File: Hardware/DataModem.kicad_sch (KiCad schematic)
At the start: 33 parts, among them J1 5V, J2 SERIAL, J3 DB9 FEMALE (DCE), J4 OUT, J5 IN, Q1 2N3904, U1 MAX232, U2 LM555, U3 LM555, U4 LM358

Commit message: Add PCB
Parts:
- C1, C10, C11, C2, C3, C4, C5, C6, C7, C8, C9: footprint (none) -> Capacitor_THT:C_Disc_D5.0mm_W2.5mm_P2.50mm
- J1: footprint (none) -> Connector_BarrelJack:BarrelJack_CUI_PJ-063AH_Horizontal
- J2: footprint (none) -> Connector_PinHeader_2.54mm:PinHeader_1x04_P2.54mm_Horizontal
- J4, J5: footprint (none) -> DataModem Parts:SWITCHCRAFT_PJRAN1X1U02X
- R1, R2, R3, R4, R5, R6, R7, R8, R9: footprint (none) -> Resistor_THT:R_Axial_DIN0204_L3.6mm_D1.6mm_P5.08mm_Horizontal
- RV1, RV2: footprint (none) -> DataModem Parts:3386F-1-103LF
- U1: footprint (none) -> Package_DIP:DIP-16_W7.62mm_Socket_LongPads
- U4: footprint (none) -> Package_DIP:DIP-8_W7.62mm
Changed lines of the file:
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@@
 			)
 		)
-		(property "Footprint" ""
+		(property "Footprint" "DataModem Parts:SWITCHCRAFT_PJRAN1X1U02X"
 			(at 257.81 130.81 0)
 			(effects
@@
 			)
 		)
-		(property "Footprint" ""
+		(property "Footprint" "Resistor_THT:R_Axial_DIN0204_L3.6mm_D1.6mm_P5.08mm_Horizontal"
 			(at 189.23 138.938 90)
 			(effects
@@
 			)
 		)
-		(property "Footprint" ""
+		(property "Footprint" "Capacitor_THT:C_Disc_D5.0mm_W2.5mm_P2.50mm"
 			(at 145.7452 129.54 0)
 			(effects
@@
 			)
 		)
-		(property "Footprint" ""
+		(property "Footprint" "Capacitor_THT:C_Disc_D5.0mm_W2.5mm_P2.50mm"
 			(at 120.3452 140.97 0)
 			(effects
@@
 			)
 		)
-		(property "Footprint" ""
+		(property "Footprint" "Capacitor_THT:C_Disc_D5.0mm_W2.5mm_P2.50mm"
 			(at 123.19 145.0848 0)
 			(effects
@@
 			)
 		)
-		(property "Footprint" ""
+		(property "Footprint" "Package_DIP:DIP-8_W7.62mm"
 			(at 215.9 55.88 0)
 			(effects
@@
 			)
 		)
-		(property "Footprint" ""
+		(property "Footprint" "Resistor_THT:R_Axial_DIN0204_L3.6mm_D1.6mm_P5.08mm_Horizontal"
 			(at 224.282 101.6 90)
 			(effects
@@
 			)
 		)
-		(property "Footprint" ""
+		(property "Footprint" "Connector_BarrelJack:BarrelJack_CUI_PJ-063AH_Horizontal"
 			(at 45.72 48.006 0)
 			(effects
@@
 			)
 		)
-		(property "Footprint" ""
+		(property "Footprint" "Capacitor_THT:C_Disc_D5.0mm_W2.5mm_P2.50mm"
 			(at 123.19 152.7048 0)
 			(effects
@@
 			)
 		)
-		(property "Footprint" ""
+		(property "Footprint" "Resistor_THT:R_Axial_DIN0204_L3.6mm_D1.6mm_P5.08mm_Horizontal"
 			(at 234.442 101.6 90)
 			(effects
@@
 			)
 		)
-		(property "Footprint" ""
+		(property "Footprint" "Resistor_THT:R_Axial_DIN0204_L3.6mm_D1.6mm_P5.08mm_Horizontal"
 			(at 121.412 49.53 90)
 			(effects
@@
 			)
 		)
-		(property "Footprint" ""
+		(property "Footprint" "Capacitor_THT:C_Disc_D5.0mm_W2.5mm_P2.50mm"
 			(at 68.2752 53.34 0)
 			(effects
@@
 			)
 		)
-		(property "Footprint" ""
+		(property "Footprint" "Package_DIP:DIP-8_W7.62mm"
 			(at 46.99 168.91 0)
 			(effects
@@
 			)
 		)
-		(property "Footprint" ""
+		(property "Footprint" "Package_DIP:DIP-8_W7.62mm"
 			(at 214.63 128.27 0)
 			(effects
@@
 			)
 		)
-		(property "Footprint" ""
+		(property "Footprint" "DataModem Parts:SWITCHCRAFT_PJRAN1X1U02X"
 			(at 257.81 55.88 0)
 			(effects
@@
 			)
 		)
-		(property "Footprint" ""
+		(property "Footprint" "Resistor_THT:R_Axial_DIN0204_L3.6mm_D1.6mm_P5.08mm_Horizontal"
 			(at 224.282 143.51 90)
 			(effects
@@
 			)
 		)
-		(property "Footprint" ""
+		(property "Footprint" "Capacitor_THT:C_Disc_D5.0mm_W2.5mm_P2.50mm"
 			(at 241.3 131.7752 0)
 			(effects
@@
 			)
 		)
-		(property "Footprint" ""
+		(property "Footprint" "Capacitor_THT:C_Disc_D5.0mm_W2.5mm_P2.50mm"
 			(at 247.65 54.9148 0)
 			(effects
@@
 			)
 		)
-		(property "Footprint" ""
+		(property "Footprint" "Resistor_THT:R_Axial_DIN0204_L3.6mm_D1.6mm_P5.08mm_Horizontal"
 			(at 234.442 143.51 90)
 			(effects
@@
 					(size 1.27 1.27)
 				)
-				(hide yes)
 			)
 		)
@@
 			)
 		)
-		(property "Footprint" ""
+		(property "Footprint" "Capacitor_THT:C_Disc_D5.0mm_W2.5mm_P2.50mm"
 			(at 68.2752 140.97 0)
 			(effects
@@
 			)
 		)
-		(property "Footprint" ""
+		(property "Footprint" "DataModem Parts:3386F-1-103LF"
 			(at 201.93 137.16 0)
 			(effects
@@
 			)
 		)
-		(property "Footprint" ""
+		(property "Footprint" "Package_DIP:DIP-16_W7.62mm_Socket_LongPads"
 			(at 93.98 182.88 0)
 			(effects
@@
 			)
 		)
-		(property "Footprint" ""
+		(property "Footprint" "Resistor_THT:R_Axial_DIN0204_L3.6mm_D1.6mm_P5.08mm_Horizontal"
 			(at 121.412 29.21 90)
 			(effects
@@
 			)
 		)
-		(property "Footprint" ""
+		(property "Footprint" "Connector_PinHeader_2.54mm:PinHeader_1x04_P2.54mm_Horizontal"
 			(at 44.45 73.66 0)
 			(effects
@@
 			)
 		)
-		(property "Footprint" ""
+		(property "Footprint" "Resistor_THT:R_Axial_DIN0204_L3.6mm_D1.6mm_P5.08mm_Horizontal"
 			(at 160.782 101.6 90)
 			(effects
@@
 			)
 		)
-		(property "Footprint" ""
+		(property "Footprint" "DataModem Parts:3386F-1-103LF"
 			(at 162.56 53.34 0)
 			(effects
@@
 			)
 		)
-		(property "Footprint" ""
+		(property "Footprint" "Capacitor_THT:C_Disc_D5.0mm_W2.5mm_P2.50mm"
 			(at 161.5948 128.27 0)
 			(effects
@@
 			)
 		)
-		(property "Footprint" ""
+		(property "Footprint" "Capacitor_THT:C_Disc_D5.0mm_W2.5mm_P2.50mm"
 			(at 124.1552 68.58 0)
 			(effects
@@
 			)
 		)
-		(property "Footprint" ""
+		(property "Footprint" "Resistor_THT:R_Axial_DIN0204_L3.6mm_D1.6mm_P5.08mm_Horizontal"
 			(at 174.752 101.6 90)
 			(effects
@@
 			)
 		)
-		(property "Footprint" ""
+		(property "Footprint" "Capacitor_THT:C_Disc_D5.0mm_W2.5mm_P2.50mm"
 			(at 145.7452 66.04 0)
 			(effects

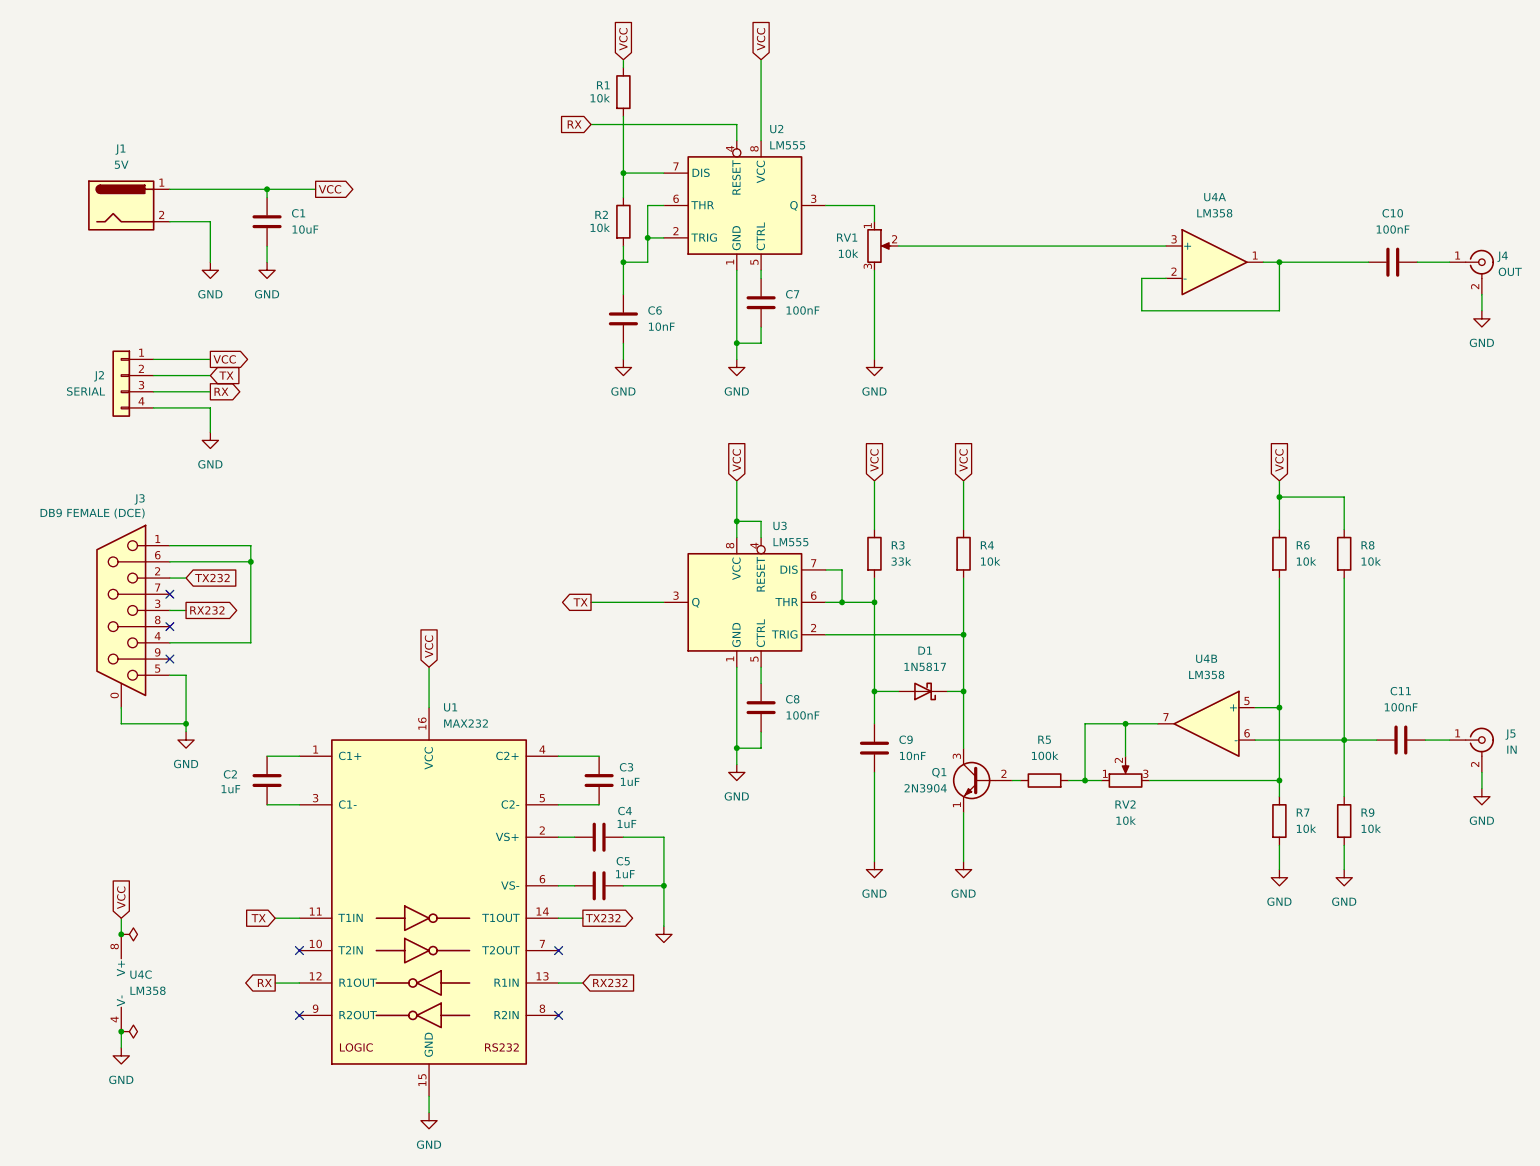
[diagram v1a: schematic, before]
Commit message: Add screw terminal for power input
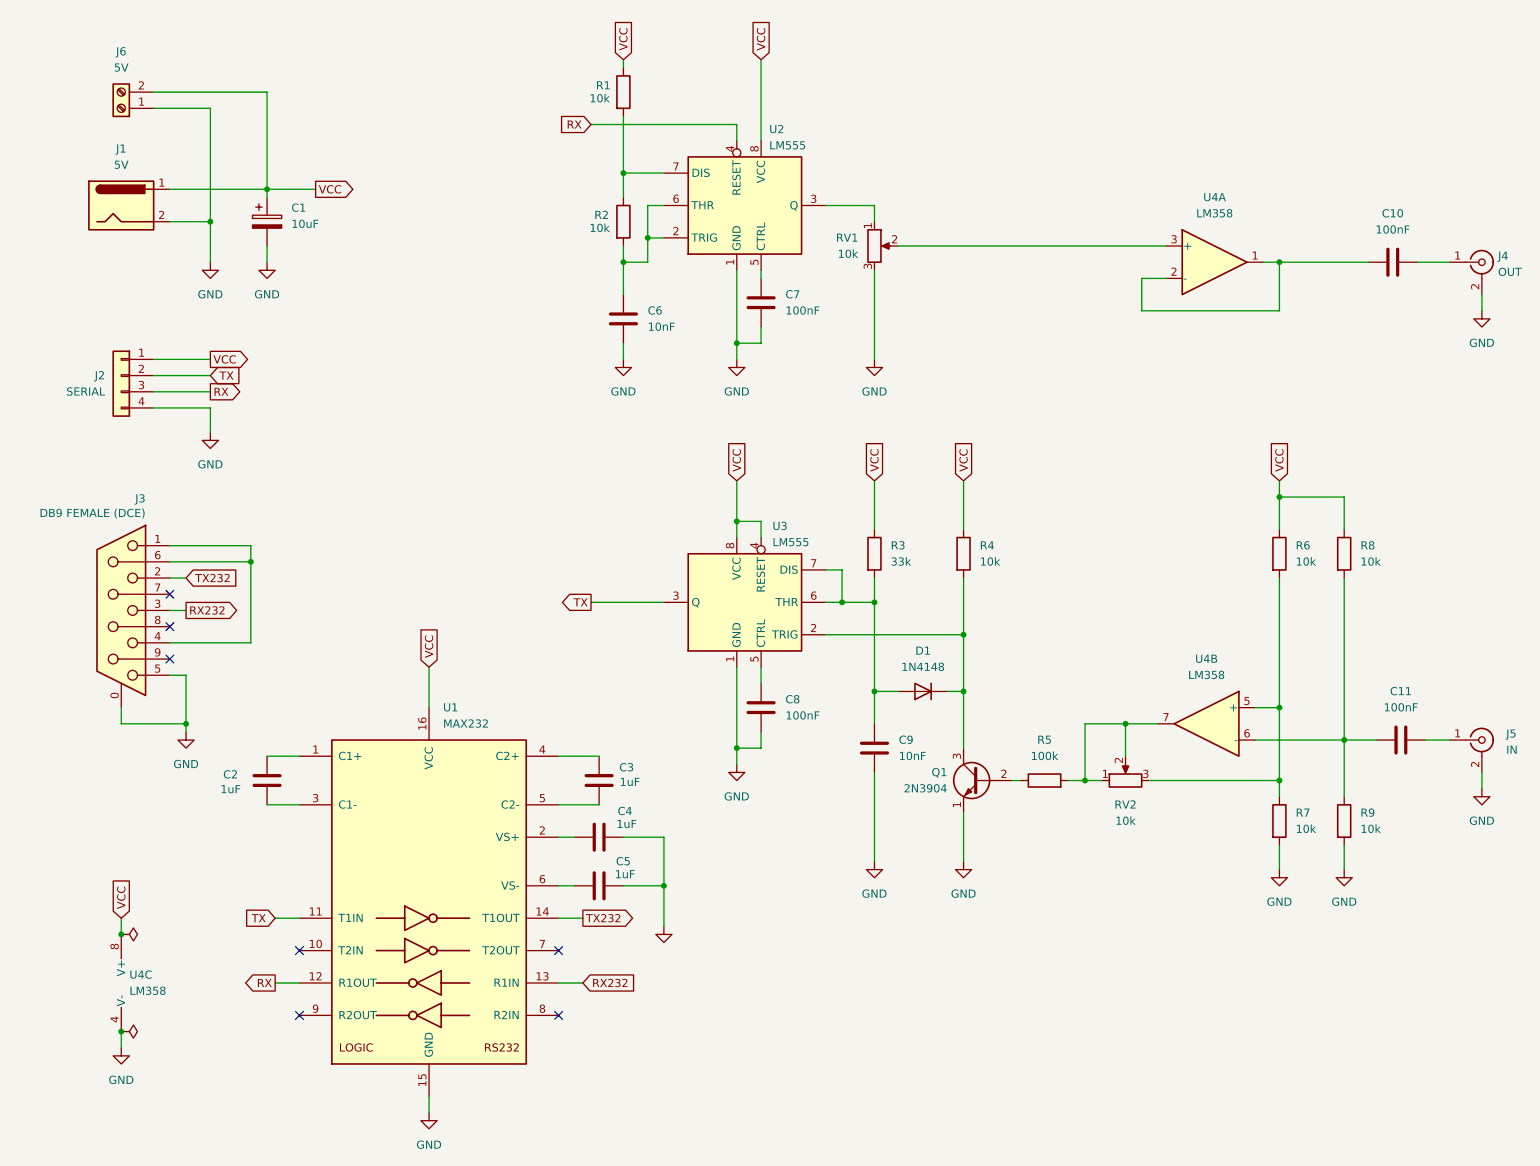
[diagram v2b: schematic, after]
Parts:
- added J6: 5V, TerminalBlock_Phoenix:TerminalBlock_Phoenix_MKDS-1,5-2-5.08_1x02_P5.08mm_Horizontal, symbol Connector:Screw_Terminal_01x02
- C1: footprint Capacitor_THT:C_Disc_D5.0mm_W2.5mm_P2.50mm -> Capacitor_THT:CP_Radial_D5.0mm_P2.50mm; symbol Device:C -> Device:C_Polarized
- D1: value 1N5817 -> 1N4148; footprint Diode_THT:D_DO-41_SOD81_P10.16mm_Horizontal -> Diode_THT:D_DO-35_SOD27_P7.62mm_Horizontal; symbol Diode:1N5817 -> Diode:1N4148
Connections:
- net GND: now also J6.1 (Pin_1)
- net VCC: now also J6.2 (Pin_2)
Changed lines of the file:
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@@
 	)
 	(junction
+		(at 58.42 49.53)
+		(diameter 0)
+		(color 0 0 0 0)
+	)
+	(junction
 		(at 195.58 137.16)
 		(diameter 0)
@@
 	(wire
 		(pts
+			(xy 58.42 31.75) (xy 58.42 49.53)
+		)
+		(stroke
+			(width 0)
+			(type default)
+		)
+	)
+	(wire
+		(pts
 			(xy 162.56 46.99) (xy 162.56 49.53)
 		)
@@
 	(wire
 		(pts
+			(xy 67.31 29.21) (xy 67.31 44.45)
+		)
+		(stroke
+			(width 0)
+			(type default)
+		)
+	)
+	(wire
+		(pts
 			(xy 157.48 109.22) (xy 154.94 109.22)
 		)
@@
 	(wire
 		(pts
+			(xy 49.53 31.75) (xy 58.42 31.75)
+		)
+		(stroke
+			(width 0)
+			(type default)
+		)
+	)
+	(wire
+		(pts
 			(xy 44.45 128.27) (xy 54.61 128.27)
 		)
@@
 	(wire
 		(pts
+			(xy 49.53 29.21) (xy 67.31 29.21)
+		)
+		(stroke
+			(width 0)
+			(type default)
+		)
+	)
+	(wire
+		(pts
 			(xy 226.06 92.71) (xy 226.06 97.79)
 		)
@@
 	)
 	(symbol
-		(lib_id "Diode:1N5817")
+		(lib_id "Diode:1N4148")
 		(at 170.18 123.19 180)
 		(unit 1)
@@
 		(fields_autoplaced yes)
 		(property "Reference" "D1"
-			(at 170.4975 116.84 0)
+			(at 170.18 116.84 0)
 			(effects
 				(font
@@
 			)
 		)
-		(property "Value" "1N5817"
-			(at 170.4975 119.38 0)
+		(property "Value" "1N4148"
+			(at 170.18 119.38 0)
 			(effects
 				(font
@@
 			)
 		)
-		(property "Footprint" "Diode_THT:D_DO-41_SOD81_P10.16mm_Horizontal"
-			(at 170.18 118.745 0)
+		(property "Footprint" "Diode_THT:D_DO-35_SOD27_P7.62mm_Horizontal"
+			(at 170.18 123.19 0)
 			(effects
 				(font
@@
 			)
 		)
-		(property "Datasheet" "http://www.vishay.com/docs/88525/1n5817.pdf"
+		(property "Datasheet" "https://assets.nexperia.com/documents/data-sheet/1N4148_1N4448.pdf"
 			(at 170.18 123.19 0)
 			(effects
@@
 			)
 		)
-		(property "Description" "20V 1A Schottky Barrier Rectifier Diode, DO-41"
+		(property "Description" "100V 0.15A standard switching diode, DO-35"
+			(at 170.18 123.19 0)
+			(effects
+				(font
+					(size 1.27 1.27)
+				)
+				(hide yes)
+			)
+		)
+		(property "Sim.Device" "D"
+			(at 170.18 123.19 0)
+			(effects
+				(font
+					(size 1.27 1.27)
+				)
+				(hide yes)
+			)
+		)
+		(property "Sim.Pins" "1=K 2=A"
 			(at 170.18 123.19 0)
 			(effects
@@
 	)
 	(symbol
-		(lib_id "Device:C")
+		(lib_id "Device:C_Polarized")
 		(at 67.31 49.53 0)
 		(unit 1)
@@
 		(fields_autoplaced yes)
 		(property "Reference" "C1"
-			(at 71.12 48.2599 0)
+			(at 71.12 47.3709 0)
 			(effects
 				(font
@@
 		)
 		(property "Value" "10uF"
-			(at 71.12 50.7999 0)
+			(at 71.12 49.9109 0)
 			(effects
 				(font
@@
 			)
 		)
-		(property "Footprint" "Capacitor_THT:C_Disc_D5.0mm_W2.5mm_P2.50mm"
+		(property "Footprint" "Capacitor_THT:CP_Radial_D5.0mm_P2.50mm"
 			(at 68.2752 53.34 0)
 			(effects
@@
 			)
 		)
-		(property "Description" "Unpolarized capacitor"
+		(property "Description" "Polarized capacitor"
 			(at 67.31 49.53 0)
 			(effects
@@
 					(unit 1)
 				)
+			)
+		)
+	)
+	(symbol
+		(lib_id "Connector:Screw_Terminal_01x02")
+		(at 44.45 31.75 180)
+		(unit 1)
+		(exclude_from_sim no)
+		(in_bom yes)
+		(on_board yes)
+		(dnp no)
+		(fields_autoplaced yes)
+		(property "Reference" "J6"
+			(at 44.45 22.86 0)
+			(effects
+				(font
+					(size 1.27 1.27)
+				)
+			)
+		)
+		(property "Value" "5V"
+			(at 44.45 25.4 0)
+			(effects
+				(font
+					(size 1.27 1.27)
+				)
+			)
+		)
+		(property "Footprint" "TerminalBlock_Phoenix:TerminalBlock_Phoenix_MKDS-1,5-2-5.08_1x02_P5.08mm_Horizontal"
+			(at 44.45 31.75 0)
+			(effects
+				(font
+					(size 1.27 1.27)
+				)
+				(hide yes)
+			)
+		)
+		(property "Datasheet" "~"
+			(at 44.45 31.75 0)
+			(effects
+				(font
+					(size 1.27 1.27)
+				)
+				(hide yes)
+			)
+		)
+		(property "Description" "Generic screw terminal, single row, 01x02, script generated (kicad-library-utils/schlib/autogen/connector/)"
+			(at 44.45 31.75 0)
+			(effects
+				(font
+					(size 1.27 1.27)
+				)
+				(hide yes)
+			)
+		)
+		(pin "2"
+		)
+		(pin "1"
+		)
+		(instances
+			(project ""
+				(path "/d925f254-ca17-48d7-83c3-bba3bac14300"
+					(reference "J6")
+					(unit 1)
+				)
